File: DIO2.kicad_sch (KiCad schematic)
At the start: 30 parts, among them J14 CD1/CD2, J15 CF/MD, J16 IN1/IN2, J17 IN3/IN4, J7 DI-2, J8 DO-2, U1 TLP627-2, U2 TLP627-2, U3 TLP627-2, U4 TLP627-2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

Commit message: カフコントローラ
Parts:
- J14, J15, J16, J17: footprint Connector_PinHeader_1.27mm:PinHeader_1x09_P1.27mm_Vertical -> Connector_PinHeader_2.54mm:PinHeader_1x09_P2.54mm_Vertical
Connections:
- net GND: no longer J8.9 (Pin_9)
- net +5V renamed COM2
- net COM2: no longer J8.10 (Pin_10)
- new net MCOM3: J8.9 (Pin_9)
- new net PCOM3: J8.10 (Pin_10)

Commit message: コネクタをピンヘッダに変更
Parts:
- J7, J8: footprint Connector_Phoenix_MC:PhoenixContact_MC_1,5_10-G-3.81_1x10_P3.81mm_Horizontal -> Connector_PinHeader_2.54mm:PinHeader_1x10_P2.54mm_Vertical
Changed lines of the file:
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@@
       (effects (font (size 1.27 1.27)))
     )
-    (property "Footprint" "Connector_Phoenix_MC:PhoenixContact_MC_1,5_10-G-3.81_1x10_P3.81mm_Horizontal" (at 168.91 59.69 0)
+    (property "Footprint" "Connector_PinHeader_2.54mm:PinHeader_1x10_P2.54mm_Vertical" (at 168.91 59.69 0)
       (effects (font (size 1.27 1.27)) hide)
     )
@@
       (effects (font (size 1.27 1.27)))
     )
-    (property "Footprint" "Connector_Phoenix_MC:PhoenixContact_MC_1,5_10-G-3.81_1x10_P3.81mm_Horizontal" (at 27.94 46.99 0)
-      (effects (font (size 1.27 1.27)) hide)
-    )
+    (property "Footprint" "Connector_PinHeader_2.54mm:PinHeader_1x10_P2.54mm_Vertical" (at 27.94 46.99 0)
+      (effects (font (size 1.27 1.27)) hide)
+    )

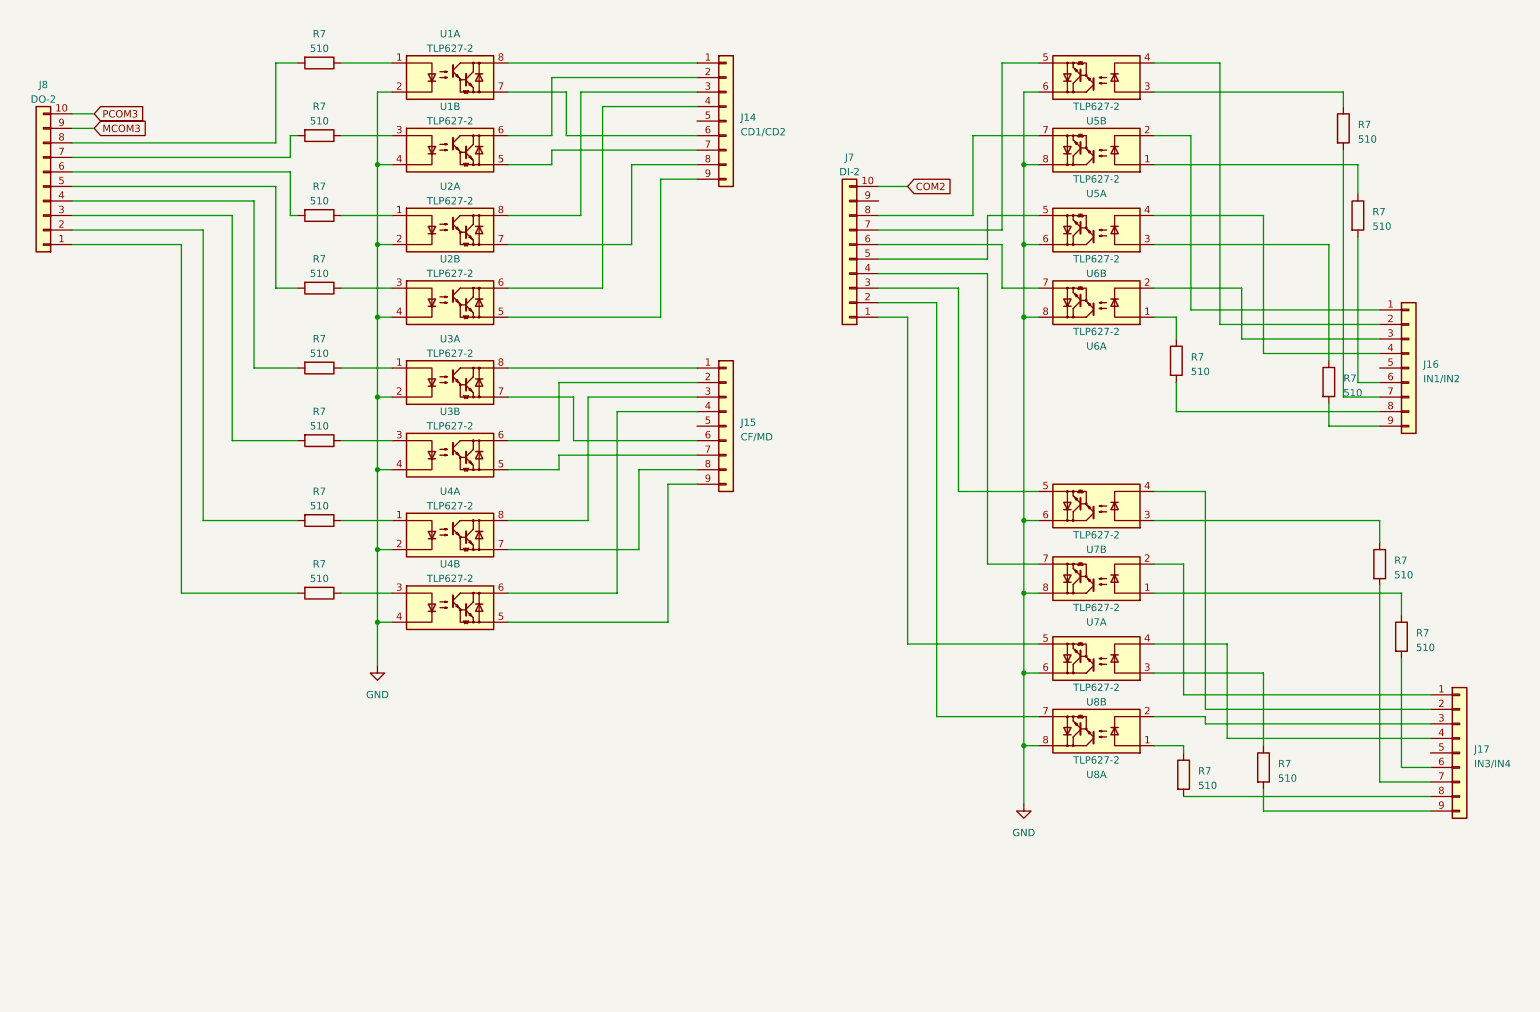
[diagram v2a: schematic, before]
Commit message: 端子をピンヘッダ2x10に変更
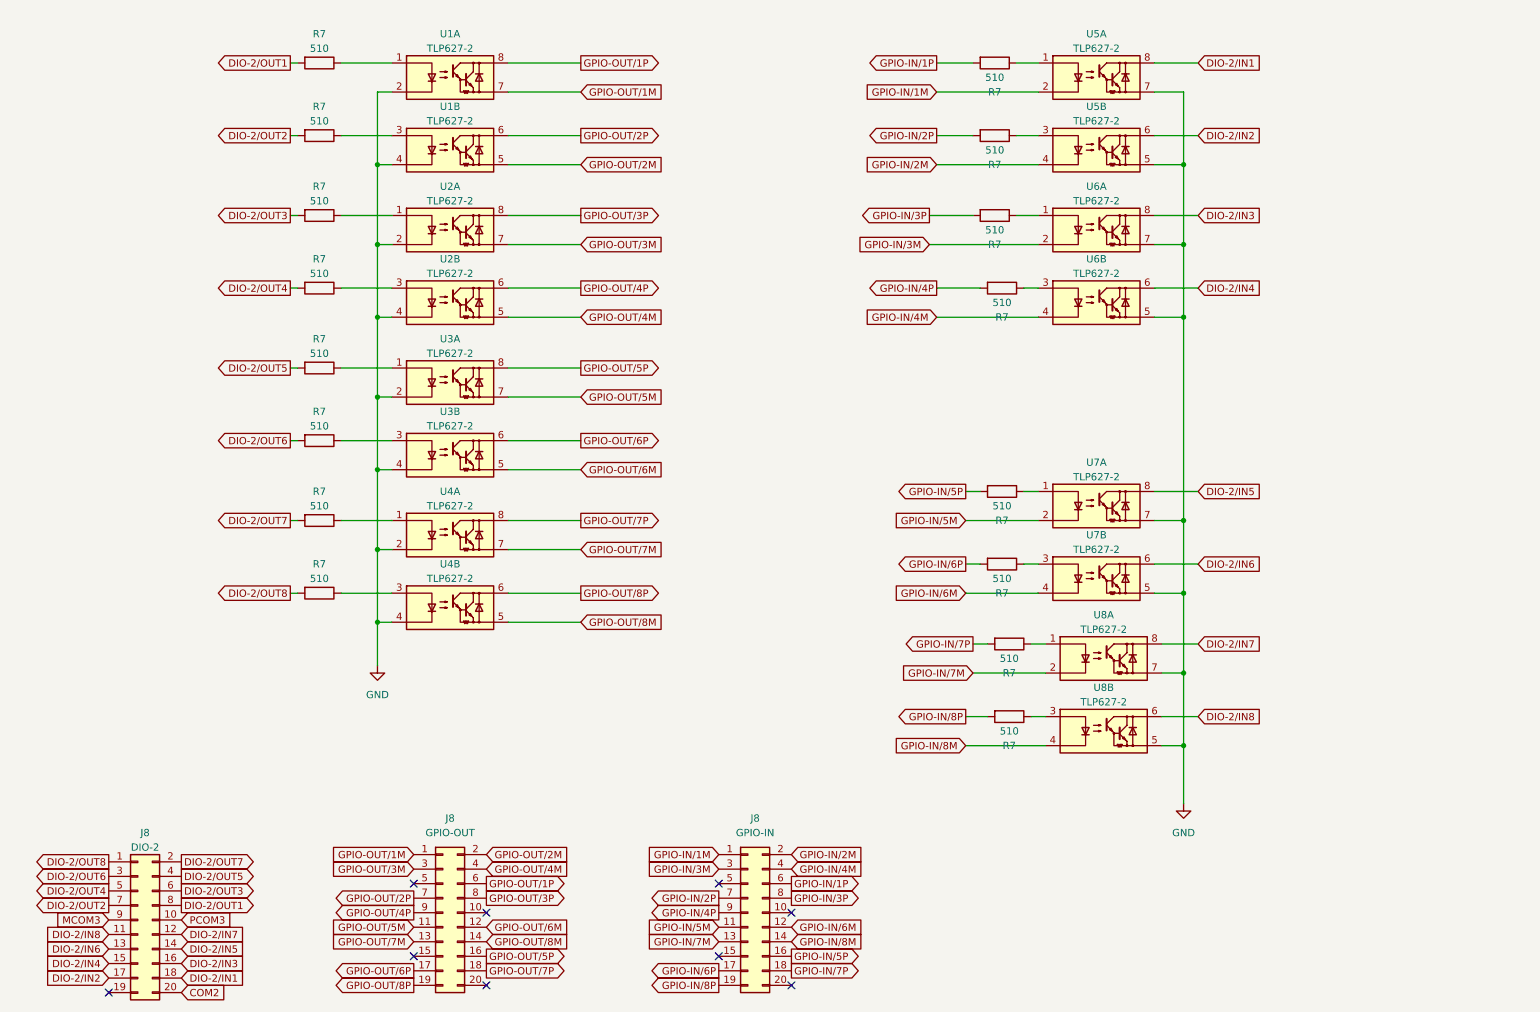
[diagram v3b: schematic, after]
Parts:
- removed J14: CD1/CD2, Connector_PinHeader_2.54mm:PinHeader_1x09_P2.54mm_Vertical, symbol Connector_Generic:Conn_01x09
- removed J15: CF/MD, Connector_PinHeader_2.54mm:PinHeader_1x09_P2.54mm_Vertical, symbol Connector_Generic:Conn_01x09
- removed J16: IN1/IN2, Connector_PinHeader_2.54mm:PinHeader_1x09_P2.54mm_Vertical, symbol Connector_Generic:Conn_01x09
- removed J17: IN3/IN4, Connector_PinHeader_2.54mm:PinHeader_1x09_P2.54mm_Vertical, symbol Connector_Generic:Conn_01x09
- removed J7: DI-2, Connector_PinHeader_2.54mm:PinHeader_1x10_P2.54mm_Vertical, symbol Connector_Generic:Conn_01x10
- removed J8: DO-2, Connector_PinHeader_2.54mm:PinHeader_1x10_P2.54mm_Vertical, symbol Connector_Generic:Conn_01x10
- added J8: GPIO-IN, Connector_PinHeader_2.54mm:PinHeader_2x10_P2.54mm_Vertical, symbol Connector_Generic:Conn_02x10_Odd_Even
- added J8: DIO-2, Connector_PinHeader_2.54mm:PinHeader_2x10_P2.54mm_Vertical, symbol Connector_Generic:Conn_02x10_Odd_Even
- added J8: GPIO-OUT, Connector_PinHeader_2.54mm:PinHeader_2x10_P2.54mm_Vertical, symbol Connector_Generic:Conn_02x10_Odd_Even
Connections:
- net COM2: now also J8.20 (Pin_20)
- net GND: now also U5.5, U5.7, U6.5, U6.7, U7.5, U7.7, U8.5, U8.7; no longer U5.6, U5.8, U6.6, U6.8, U7.6, U7.8, U8.6, U8.8
- net MCOM3: now also J8.9 (Pin_9)
- net PCOM3: now also J8.10 (Pin_10)
- net GPIO-IN/3P: now reaches R7.2
- net GPIO-IN/3P: now also J8.8 (Pin_8)
- net GPIO-IN/4M: now reaches U6.4
- net GPIO-IN/4M: now also J8.4 (Pin_4)
- net at U7.1: now also R7.1; no longer R7.1
- net GPIO-IN/5M: now reaches U7.2
- net GPIO-IN/5M: now also J8.11 (Pin_11)
- net DIO-2/OUT3: now reaches R7.2
- net DIO-2/OUT3: now also J8.6 (Pin_6)
- net GPIO-OUT/1P: now reaches U1.8
- net GPIO-OUT/1P: now also J8.6 (Pin_6)
- net GPIO-OUT/2P: now reaches U1.6
- net GPIO-OUT/2P: now also J8.7 (Pin_7)
- net GPIO-OUT/3P: now reaches U2.8
- net GPIO-OUT/3P: now also J8.8 (Pin_8)
- net GPIO-OUT/4P: now reaches U2.6
- net GPIO-OUT/4P: now also J8.9 (Pin_9)
- net GPIO-OUT/1M: now reaches U1.7
- net GPIO-OUT/1M: now also J8.1 (Pin_1)
- net GPIO-OUT/2M: now reaches U1.5
- net GPIO-OUT/2M: now also J8.2 (Pin_2)
- net GPIO-OUT/3M: now reaches U2.7
- net GPIO-OUT/3M: now also J8.3 (Pin_3)
- net GPIO-OUT/4M: now reaches U2.5
- net GPIO-OUT/4M: now also J8.4 (Pin_4)
- net GPIO-IN/4P: now reaches R7.2
- net GPIO-IN/4P: now also J8.9 (Pin_9)
- net at U7.3: now also R7.1; no longer R7.1
- net GPIO-IN/5P: now reaches R7.2
- net GPIO-IN/5P: now also J8.16 (Pin_16)
- net GPIO-OUT/6M: now reaches U3.5
- net GPIO-OUT/6M: now also J8.12 (Pin_12)
- net GPIO-OUT/6P: now reaches U3.6
- net GPIO-OUT/6P: now also J8.17 (Pin_17)
- net GPIO-OUT/5P: now reaches U3.8
- net GPIO-OUT/5P: now also J8.16 (Pin_16)
- net GPIO-OUT/7P: now reaches U4.8
- net GPIO-OUT/7P: now also J8.18 (Pin_18)
- net GPIO-OUT/8P: now reaches U4.6
- net GPIO-OUT/8P: now also J8.19 (Pin_19)
- net GPIO-OUT/5M: now reaches U3.7
- net GPIO-OUT/5M: now also J8.11 (Pin_11)
- net GPIO-OUT/7M: now reaches U4.7
- net GPIO-OUT/7M: now also J8.13 (Pin_13)
- net GPIO-OUT/8M: now reaches U4.5
- net GPIO-OUT/8M: now also J8.14 (Pin_14)
- net DIO-2/OUT1: now reaches R7.2
- net DIO-2/OUT1: now also J8.8 (Pin_8)
- net GPIO-IN/2M: now reaches U5.4
- net GPIO-IN/2M: now also J8.2 (Pin_2)
- net at U8.1: now also R7.1; no longer R7.1
- net GPIO-IN/7M: now reaches U8.2
- net GPIO-IN/7M: now also J8.13 (Pin_13)
- net DIO-2/OUT7: now reaches R7.2
- net DIO-2/OUT7: now also J8.2 (Pin_2)
- net DIO-2/OUT8: now reaches R7.2
- net DIO-2/OUT8: now also J8.1 (Pin_1)
- net DIO-2/OUT6: now reaches R7.2
- net DIO-2/OUT6: now also J8.3 (Pin_3)
- net DIO-2/OUT5: now reaches R7.2
- net DIO-2/OUT5: now also J8.4 (Pin_4)
- net DIO-2/OUT4: now reaches R7.2
- net DIO-2/OUT4: now also J8.5 (Pin_5)
- net DIO-2/OUT2: now reaches R7.2
- net DIO-2/OUT2: now also J8.7 (Pin_7)
- net GPIO-IN/3M: now reaches U6.2
- net GPIO-IN/3M: now also J8.3 (Pin_3)
- net GPIO-IN/1P: now reaches R7.2
- net GPIO-IN/1P: now also J8.6 (Pin_6)
- net GPIO-IN/6P: now reaches R7.2
- net GPIO-IN/6P: now also J8.17 (Pin_17)
- net GPIO-IN/6M: now reaches U7.4
- net GPIO-IN/6M: now also J8.12 (Pin_12)
- net GPIO-IN/8M: now reaches U8.4
- net GPIO-IN/8M: now also J8.14 (Pin_14)
- net GPIO-IN/8P: now reaches R7.2
- net GPIO-IN/8P: now also J8.19 (Pin_19)
- net GPIO-IN/7P: now reaches R7.2
- net GPIO-IN/7P: now also J8.18 (Pin_18)
- net GPIO-IN/1M: now reaches U5.2
- net GPIO-IN/1M: now also J8.1 (Pin_1)
- net at U8.3: now also R7.1; no longer R7.1
- net GPIO-IN/2P: now reaches R7.2
- net GPIO-IN/2P: now also J8.7 (Pin_7)
- new net DIO-2/IN1: J8.18 (Pin_18), U5.8
- new net DIO-2/IN2: J8.17 (Pin_17), U5.6
- new net DIO-2/IN3: J8.16 (Pin_16), U6.8
- new net DIO-2/IN4: J8.15 (Pin_15), U6.6
- new net DIO-2/IN5: J8.14 (Pin_14), U7.8
- new net DIO-2/IN6: J8.13 (Pin_13), U7.6
- new net DIO-2/IN7: J8.12 (Pin_12), U8.8
- new net DIO-2/IN8: J8.11 (Pin_11), U8.6
- no-connect marks 0 -> 9
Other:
- moved on the sheet: R7, U5A, U5B, U6A, U6B, U7A, U7B, U8A, U8B

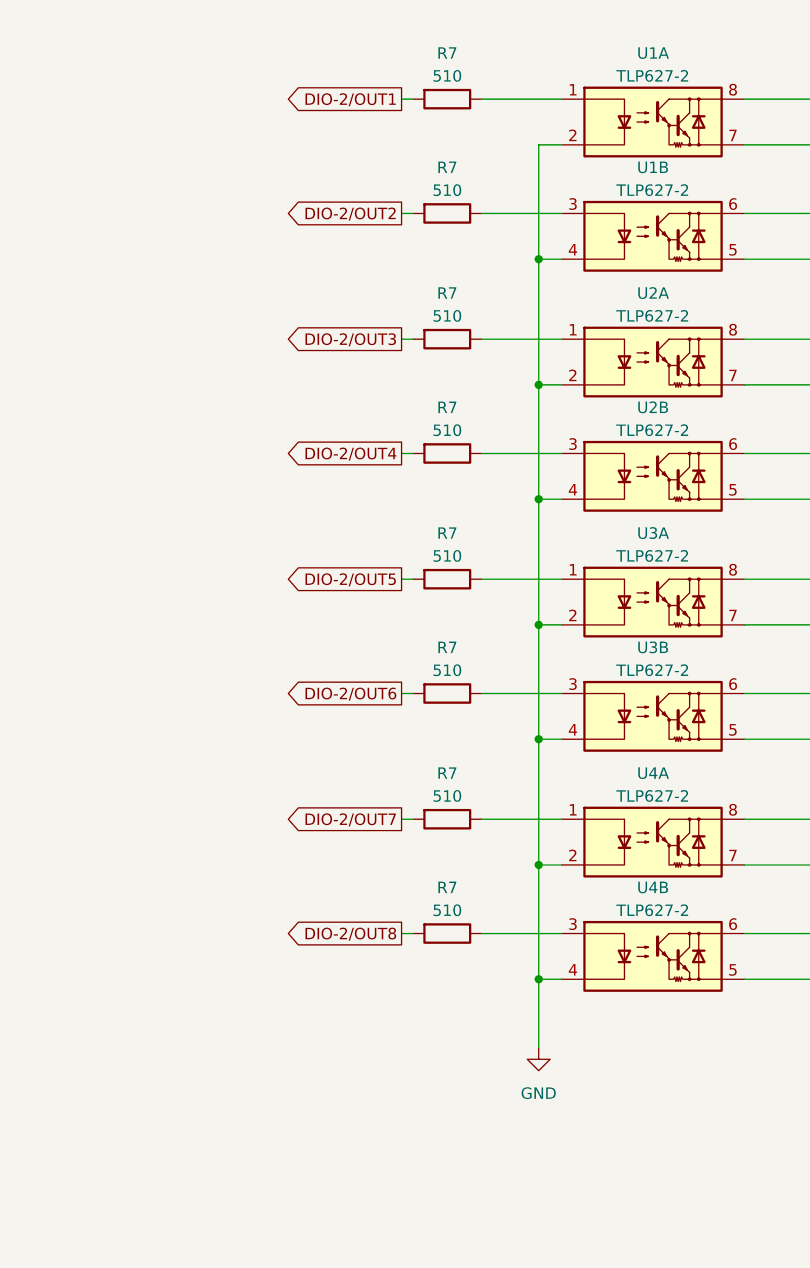
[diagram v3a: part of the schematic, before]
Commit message: GPIO OUT ジックミスを修正
電流シンクに変更
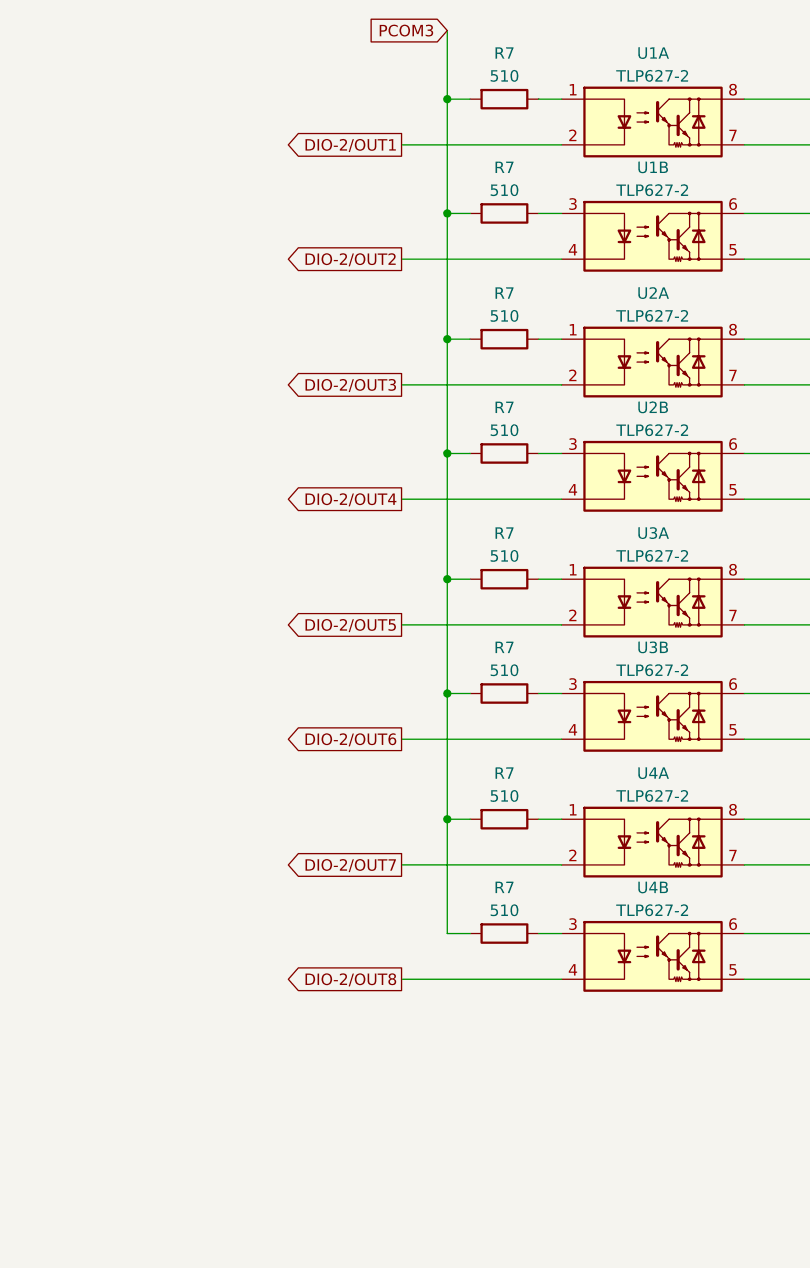
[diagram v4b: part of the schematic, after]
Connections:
- net DIO-2/OUT1: now also U1.2; no longer R7.2
- net DIO-2/OUT2: now also U1.4; no longer R7.2
- net DIO-2/OUT3: now also U2.2; no longer R7.2
- net DIO-2/OUT4: now also U2.4; no longer R7.2
- net DIO-2/OUT5: now also U3.2; no longer R7.2
- net DIO-2/OUT6: now also U3.4; no longer R7.2
- net DIO-2/OUT7: now also U4.2; no longer R7.2
- net DIO-2/OUT8: now also U4.4; no longer R7.2
- net GND: no longer U1.2, U1.4, U2.2, U2.4, U3.2, U3.4, U4.2, U4.4
- net PCOM3: now also R7.2, R7.2, R7.2, R7.2, R7.2, R7.2, R7.2, R7.2
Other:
- moved on the sheet: R7

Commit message: SW6/SW7を追加
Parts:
- J8: footprint Connector_PinHeader_2.54mm:PinHeader_2x10_P2.54mm_Vertical -> BoxHeader:BoxHeader_2x10_P2.54mm_Vertical
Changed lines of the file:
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@@
       (effects (font (size 1.27 1.27)))
     )
-    (property "Footprint" "Connector_PinHeader_2.54mm:PinHeader_2x10_P2.54mm_Vertical" (at 151.13 173.99 0)
+    (property "Footprint" "BoxHeader:BoxHeader_2x10_P2.54mm_Vertical" (at 151.13 173.99 0)
       (effects (font (size 1.27 1.27)) hide)
     )
@@
       (effects (font (size 1.27 1.27)))
     )
-    (property "Footprint" "Connector_PinHeader_2.54mm:PinHeader_2x10_P2.54mm_Vertical" (at 44.45 175.26 0)
+    (property "Footprint" "BoxHeader:BoxHeader_2x10_P2.54mm_Vertical" (at 44.45 175.26 0)
       (effects (font (size 1.27 1.27)) hide)
     )
@@
       (effects (font (size 1.27 1.27)))
     )
-    (property "Footprint" "Connector_PinHeader_2.54mm:PinHeader_2x10_P2.54mm_Vertical" (at 97.79 173.99 0)
-      (effects (font (size 1.27 1.27)) hide)
-    )
+    (property "Footprint" "BoxHeader:BoxHeader_2x10_P2.54mm_Vertical" (at 97.79 173.99 0)
+      (effects (font (size 1.27 1.27)) hide)
+    )
